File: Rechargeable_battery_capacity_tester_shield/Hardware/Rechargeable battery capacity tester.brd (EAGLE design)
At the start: 68.6 x 53.3 mm, 33 parts, among them J3 CON_HEADER_1X08-PTH, J5 CON_HEADER_1X08-PTH, Q1 IRL3103S, Q2 IRL3103S, Q3 IRL3103S

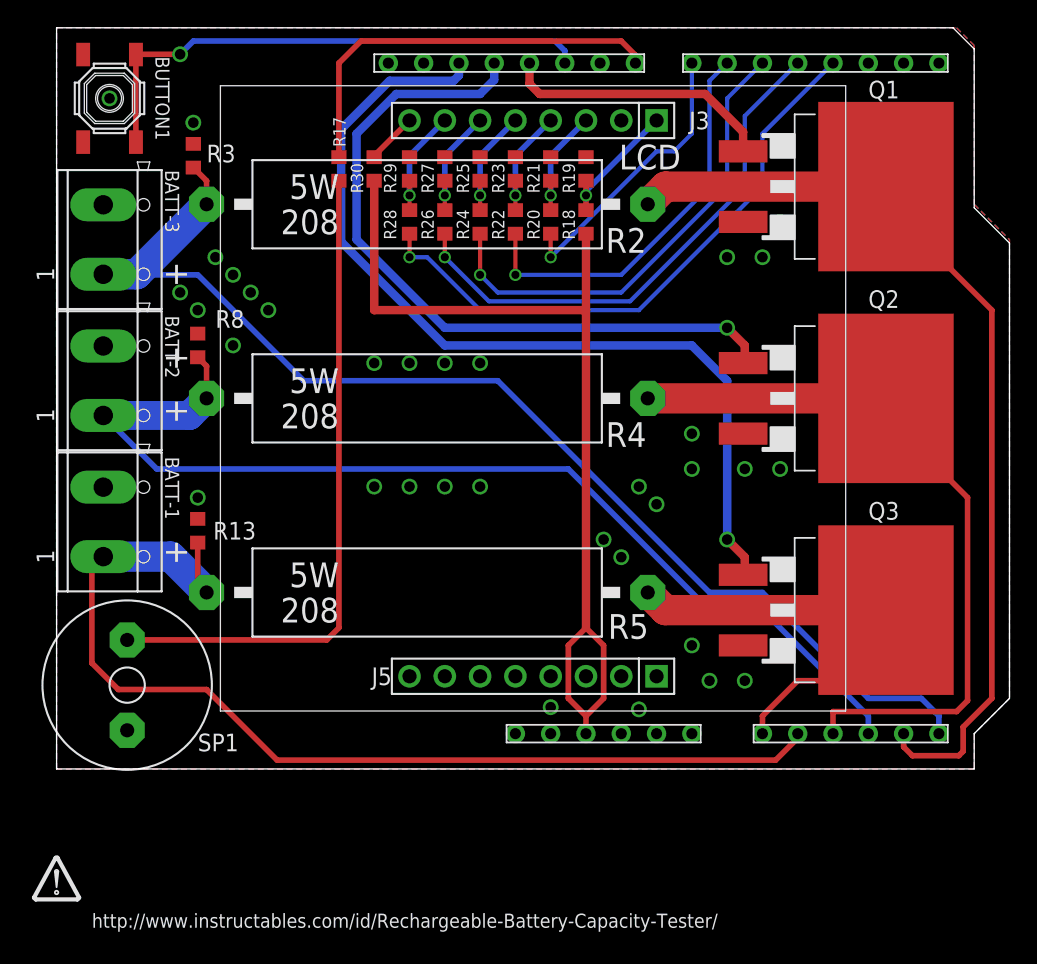
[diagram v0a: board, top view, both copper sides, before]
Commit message: -fix the overlapping resistors (R2 and LCD SMT voltage dividers resistors)
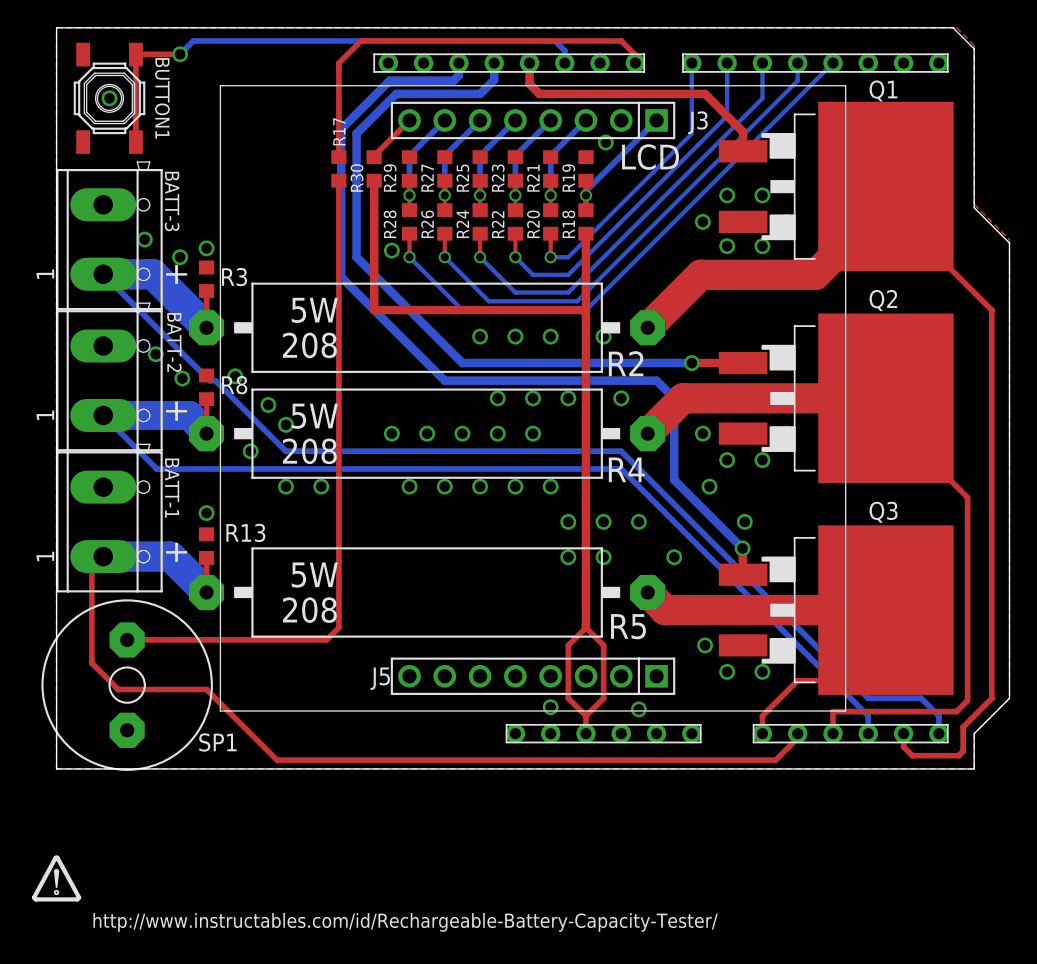
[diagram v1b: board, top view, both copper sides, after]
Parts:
- moved R3 8.94 mm to (10.8, 35.2)
- moved R2 8.89 mm to (26.7, 31.8)
- moved R8 3.08 mm to (10.8, 27.5)
- moved R4 2.54 mm to (26.7, 24.1)
- moved R13 1.28 mm to (10.8, 16.0)
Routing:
- net AD4: track 68.0 -> 73.1 mm
- net D6: track 29.0 -> 26.0 mm
- net D5: track 34.4 -> 31.4 mm
- net D3: track 43.3 -> 41.1 mm
- net D4: track 38.5 -> 36.3 mm
- net D13/SCK: track 65.5 -> 63.9 mm
- net AD1: track 75.0 -> 73.7 mm
- net AD2: track 52.9 -> 54.0 mm
- net AD5: track 87.1 -> 86.3 mm
- net AD3: track 76.5 -> 75.8 mm
